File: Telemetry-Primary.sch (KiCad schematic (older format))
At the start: 39 parts, among them J1 CAN_LogicAnalyzer, J2 IMU_LogicAnalyzer, J3 GPS_LogicAnalyzer, J4 RTCC_LogicAnalyzer, J5 SDCard_LogicAnalyzer, J6 SWD, SW1 Reset, U1 STM32F429ZITx, Y1 8M

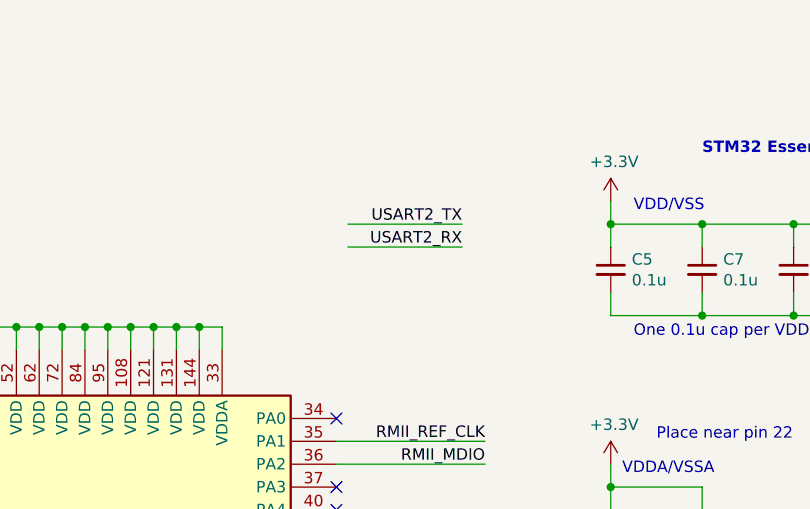
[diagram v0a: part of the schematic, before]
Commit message: Some changes to solve errata and list of errata in v1
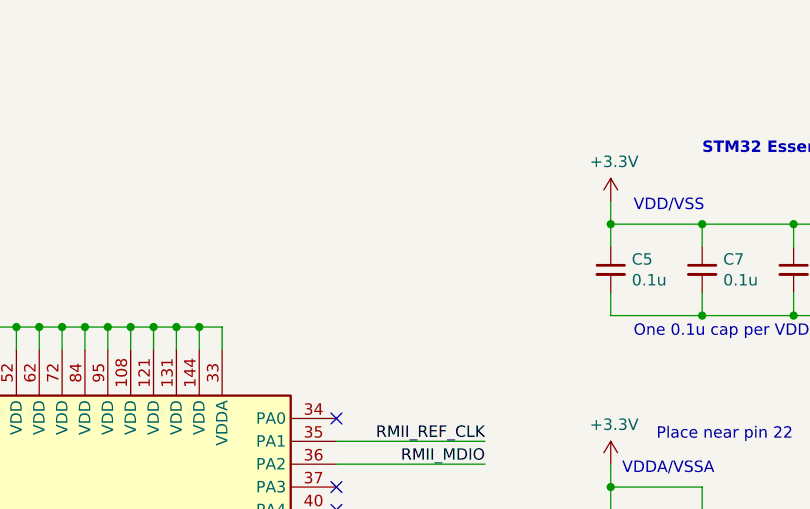
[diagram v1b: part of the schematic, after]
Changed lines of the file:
@@
 EESchema Schematic File Version 4
-LIBS:Telemetry-Primary-cache
-EELAYER 26 0
+EELAYER 30 0
 EELAYER END
 $Descr A3 16535 11693
@@
 CAN1_RX
 Wire Wire Line
-	9000 1450 9500 1450
-Wire Wire Line
-	9500 1550 9000 1550
-Wire Wire Line
 	8950 8200 9600 8200
 Wire Wire Line
@@
 Text Label 2650 2900 2    50   ~ 0
 USART3_RX
-Text Label 9500 1550 2    50   ~ 0
-USART2_RX
-Text Label 9500 1450 2    50   ~ 0
-USART2_TX
 Wire Wire Line
 	6550 6400 5900 6400
